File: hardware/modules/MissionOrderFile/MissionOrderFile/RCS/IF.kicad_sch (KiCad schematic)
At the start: 4 parts, among them J101 Jumper, J102 Conn_01x04_MountingPin

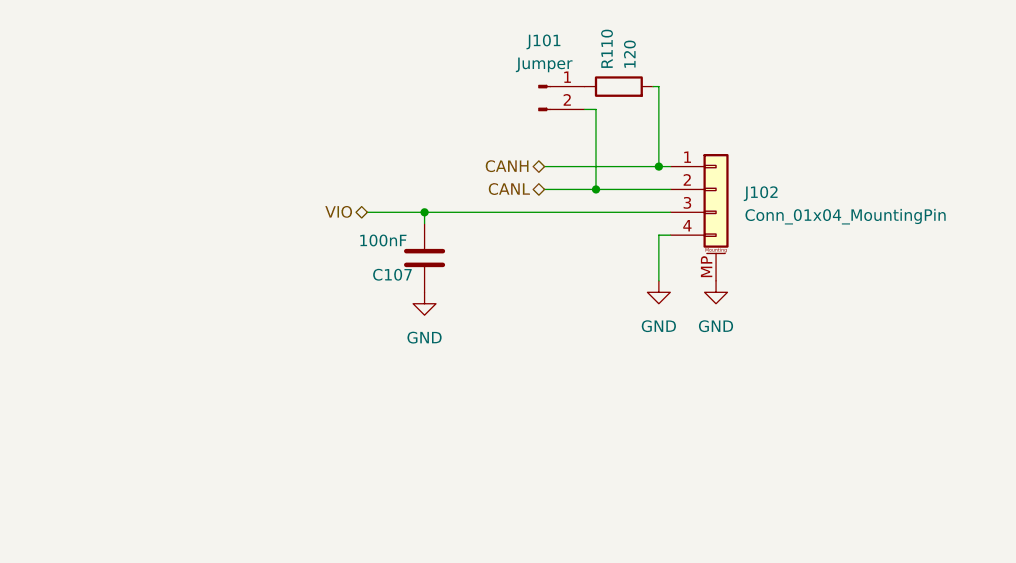
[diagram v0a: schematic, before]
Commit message: 発注基板RCSモジュール反映
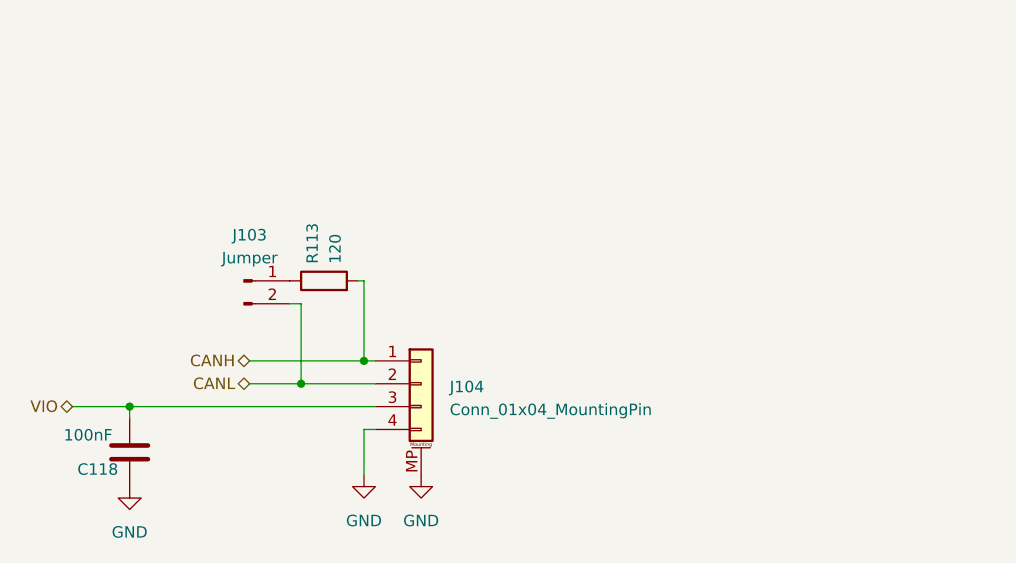
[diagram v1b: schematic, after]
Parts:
- removed C107: 100nF, Capacitor_SMD:C_0402_1005Metric, symbol Device:C
- removed J101: Jumper, Connector_PinHeader_1.27mm:PinHeader_1x02_P1.27mm_Vertical, symbol Connector:Conn_01x02_Pin
- removed J102: Conn_01x04_MountingPin, WOBCLibrary:Grove_4P_L_SMD, symbol Connector_Generic_MountingPin:Conn_01x04_MountingPin
- removed R110: 120, Resistor_SMD:R_0402_1005Metric, symbol Device:R
- added C118: 100nF, Capacitor_SMD:C_0402_1005Metric, symbol Device:C
- added J103: Jumper, Connector_PinHeader_1.27mm:PinHeader_1x02_P1.27mm_Vertical, symbol Connector:Conn_01x02_Pin
- added J104: Conn_01x04_MountingPin, WOBCLibrary:Grove_4P_L_SMD, symbol Connector_Generic_MountingPin:Conn_01x04_MountingPin
- added R113: 120, Resistor_SMD:R_0402_1005Metric, symbol Device:R
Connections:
- net CANH: now also J104.1 (Pin_1), R113.2
- net CANL: now also J103.2 (Pin_2), J104.2 (Pin_2)
- net GND: now also C118.1, J104.4 (Pin_4), J104.MP (MountPin)
- net VIO: now also C118.2, J104.3 (Pin_3)
- new net: J103.1 (Pin_1), R113.1
